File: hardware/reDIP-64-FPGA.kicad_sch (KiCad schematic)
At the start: 22 parts, among them J3 Conn_01x20, J4 Conn_01x20, J5 Conn_01x20, J6 Conn_01x20, J7 Conn_01x20, U16 SN74CBTD16211DGVR, U17 SN74CBTD16211DGVR, U18 SN74CBTD16211DGVR, U19 SN74CBTD16211DGVR, U8 LFE5UM5G-25F-8MG285C

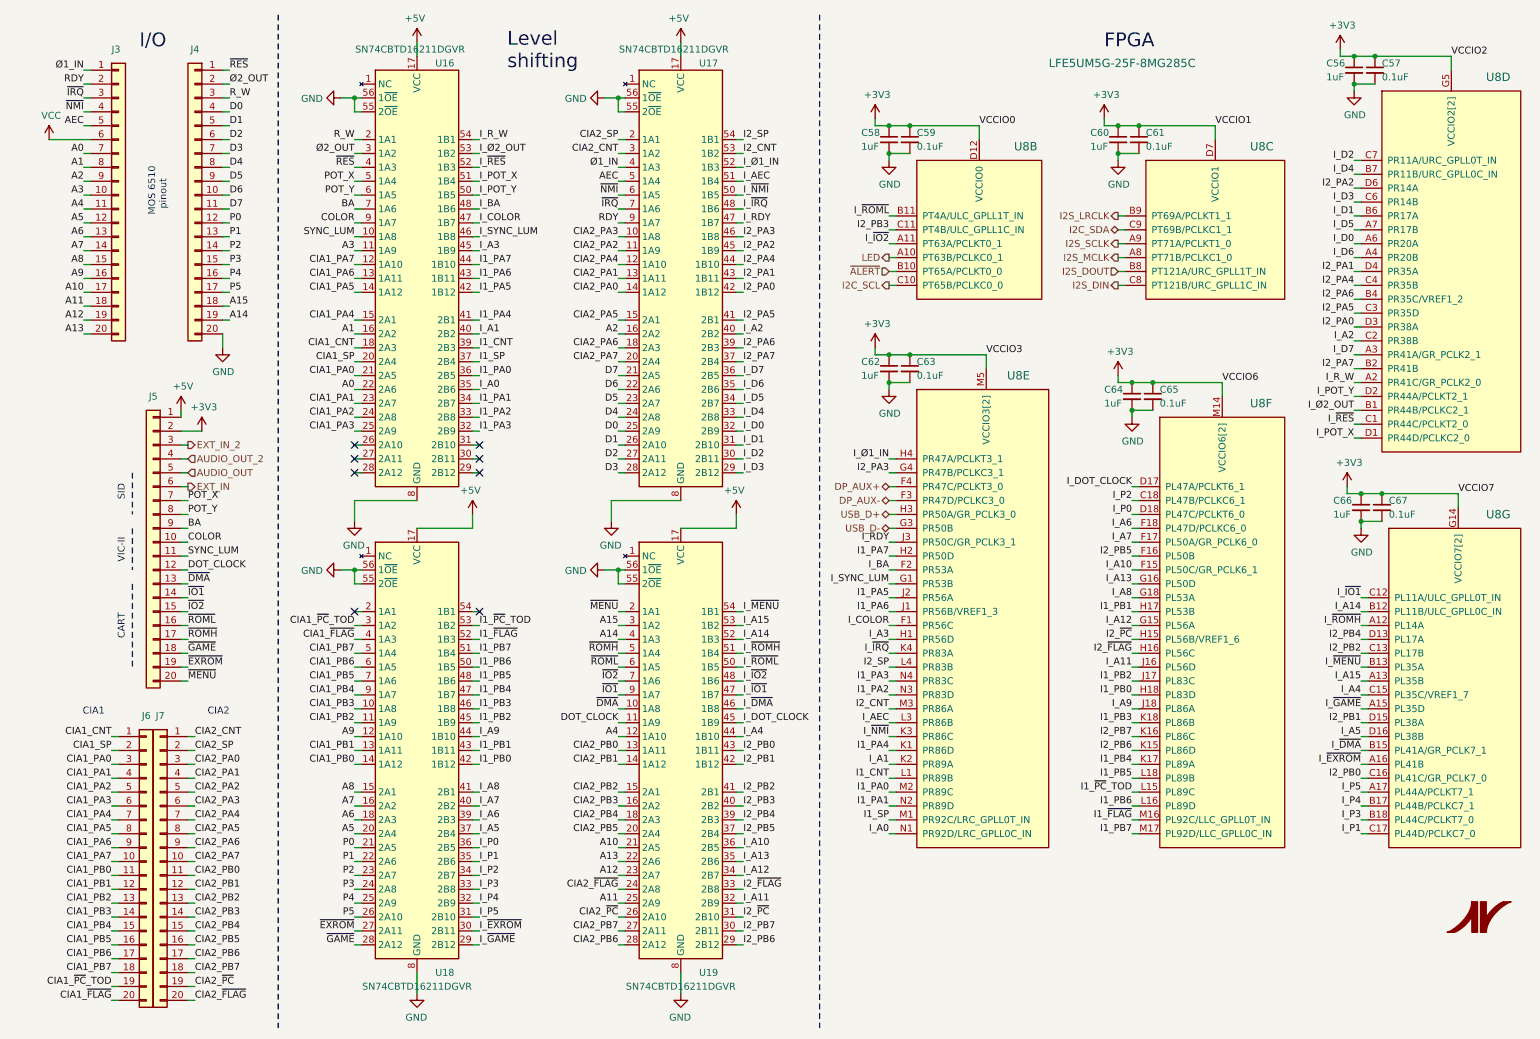
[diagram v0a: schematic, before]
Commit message: Various improvements
* Removed slash from sheet names
* Reannotated schematics
* Example derivation of clocks in schematics
* Identical capacitors for DisplayPort main lanes and AUX
* Replaced switch FSA2259UMX with FSUSB42UMX
* Modified PCB physical stackup to (hopefully) be manufacturable
* Only one microvia size (0.1mm)
* Changed track width for differential pairs
* Routing cleanups and improvements
* Added files for manufacture
* Updated README

Many thanks for advice and help go to @azonenberg, @DX-MON, @gatecat,
@smunaut, and @zyp.
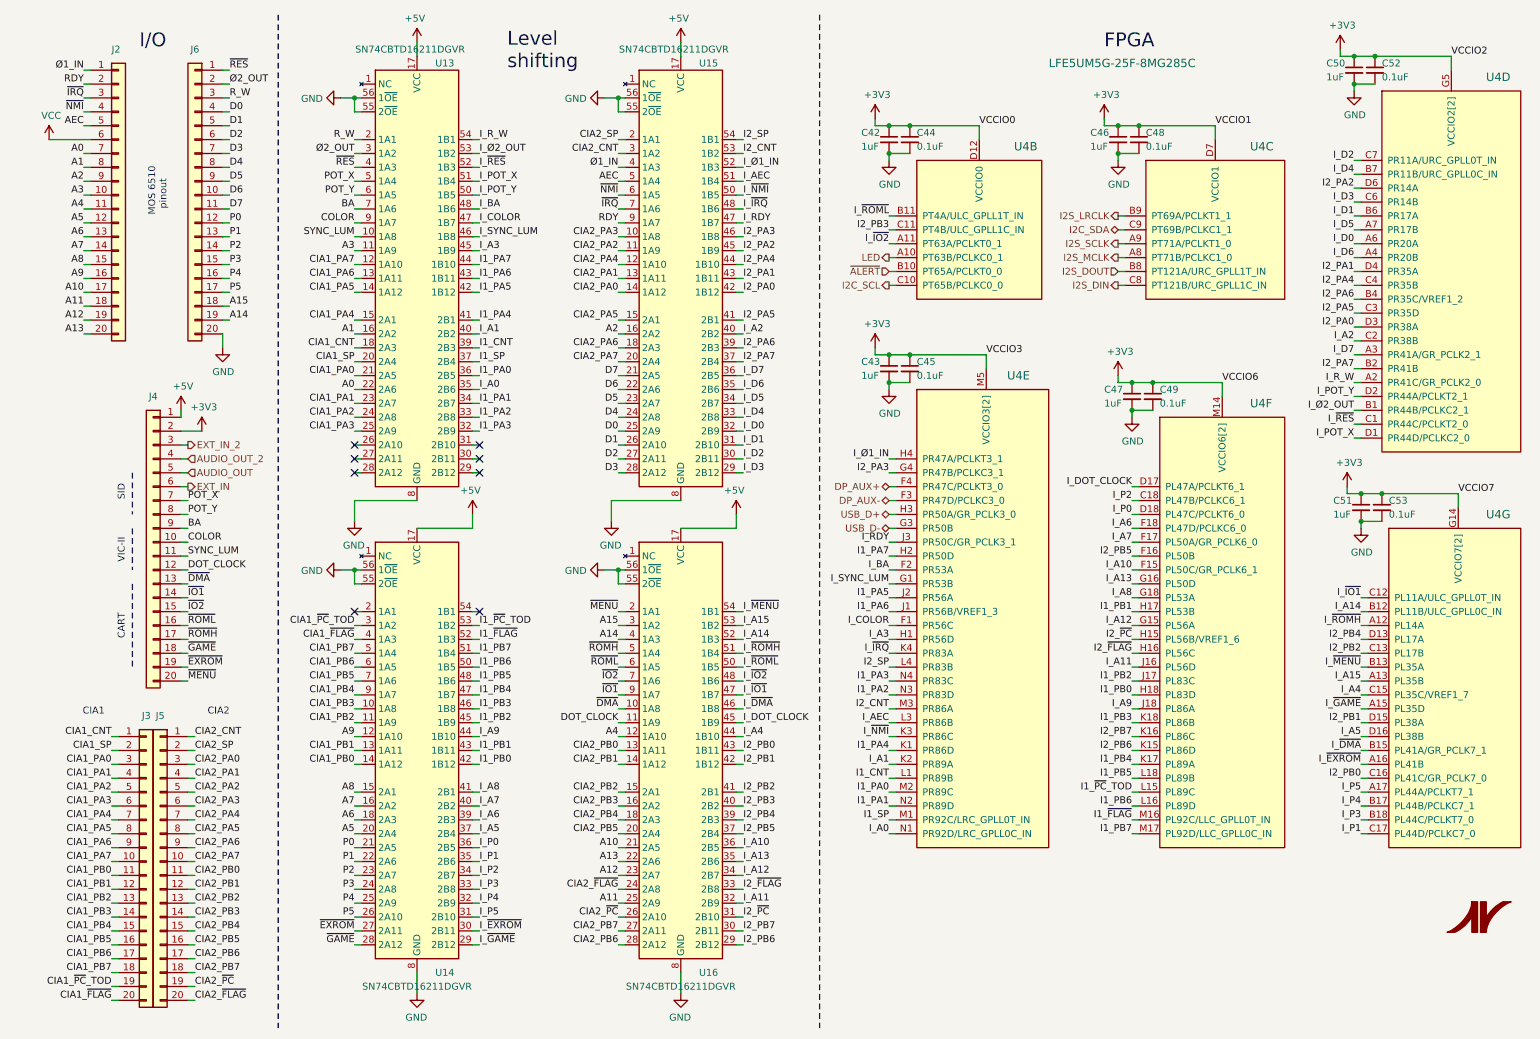
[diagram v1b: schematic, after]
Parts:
- renumbered C58 to C42, C62 to C43, C59 to C44, C63 to C45, C60 to C46, C64 to C47, C61 to C48, C65 to C49, C56 to C50, C66 to C51, C57 to C52, C67 to C53, J3 to J2, J6 to J3, J5 to J4, J7 to J5, J4 to J6, U16 to U13, U18 to U14, U17 to U15, U19 to U16, U8 to U4

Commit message: Updated all KiCad files to current format
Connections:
- net CIA1_~FLAG~ renamed CIA1_~{FLAG}
- net CIA1_~PC~_TOD renamed CIA1_~{PC}_TOD
- net CIA2_~FLAG~ renamed CIA2_~{FLAG}
- net CIA2_~PC~ renamed CIA2_~{PC}
- net I1_~FLAG~ renamed I1_~{FLAG}
- net I1_~PC~_TOD renamed I1_~{PC}_TOD
- net I2_~FLAG~ renamed I2_~{FLAG}
- net I2_~PC~ renamed I2_~{PC}
- net I_~DMA~ renamed I_~{DMA}
- net I_~EXROM~ renamed I_~{EXROM}
- net I_~GAME~ renamed I_~{GAME}
- net I_~IO1~ renamed I_~{IO1}
- net I_~IO2~ renamed I_~{IO2}
- net I_~IRQ~ renamed I_~{IRQ}
- net I_~MENU~ renamed I_~{MENU}
- net I_~NMI~ renamed I_~{NMI}
- net I_~RES~ renamed I_~{RES}
- net I_~ROMH~ renamed I_~{ROMH}
- net I_~ROML~ renamed I_~{ROML}
- net ~ALERT~ renamed ~{ALERT}
- net ~DMA~ renamed ~{DMA}
- net ~EXROM~ renamed ~{EXROM}
- net ~GAME~ renamed ~{GAME}
- net ~IO1~ renamed ~{IO1}
- net ~IO2~ renamed ~{IO2}
- net ~IRQ~ renamed ~{IRQ}
- net ~MENU~ renamed ~{MENU}
- net ~NMI~ renamed ~{NMI}
- net ~RES~ renamed ~{RES}
- net ~ROMH~ renamed ~{ROMH}
- net ~ROML~ renamed ~{ROML}

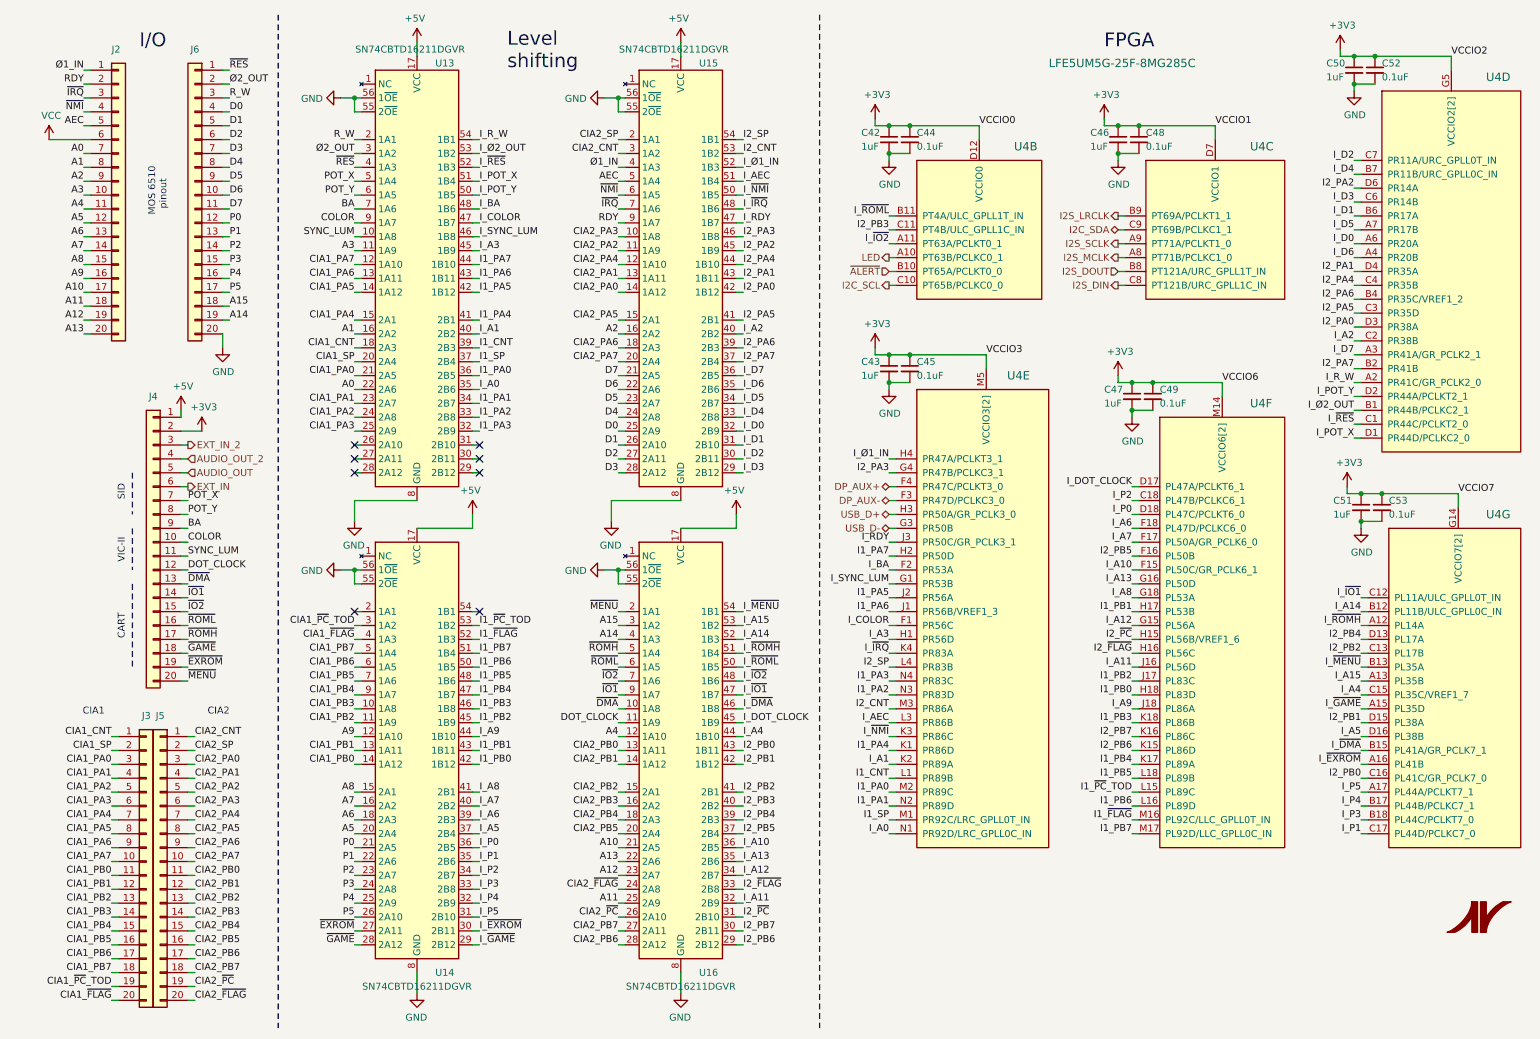
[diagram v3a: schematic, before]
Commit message: Revision 1.0
* USB receptacle replaced with GCT USB4080-03-A / HRO TYPE-C-31-M-05
* USB PD TCPC changed to PTN5110NHQ (FPF2286 has 15ms VBUS debounce time)
* Complete rework of power section
  - Over-voltage protection on VBUS (FPF2286 / FPF2495C)
  - Bidirectional VCC (2 x TPS22916)
  - Replaced EOLed buck converters with FAN53610 / FAN53611
  - Replaced EOLed LDO for ECP5 VCCAUX with NCP115AMX250TCG
  - Replaced LDO for SGTL5000 VDDA with 3.3V version
  - Added separate LDO for SGTL5000 VDDD, avoiding overvoltage on ECP5 VCC
* Bus switch changed to SN74CBT16211A, biased for level shifting
* Registered I/O for FLASH / HyperRAM clock
* Pin header changes:
  - Machined (round) pins for MOS6510 socket
  - Top only headers for additional I/O
  - Reworked pinout for VIC-II and SID
  - Removed 5V output (now available on bidirectional VCC)
  - Added GND for audio / 3.3V
  - Changed JTAG pinout to match Tag-Connect TC-LATTICE / TC-XILINX6
* Removed EXT_IN capacitors
* Button force changed from 240gf to 100gf
* Space for UL and date codes
* Black solder mask
* Silk screen updates
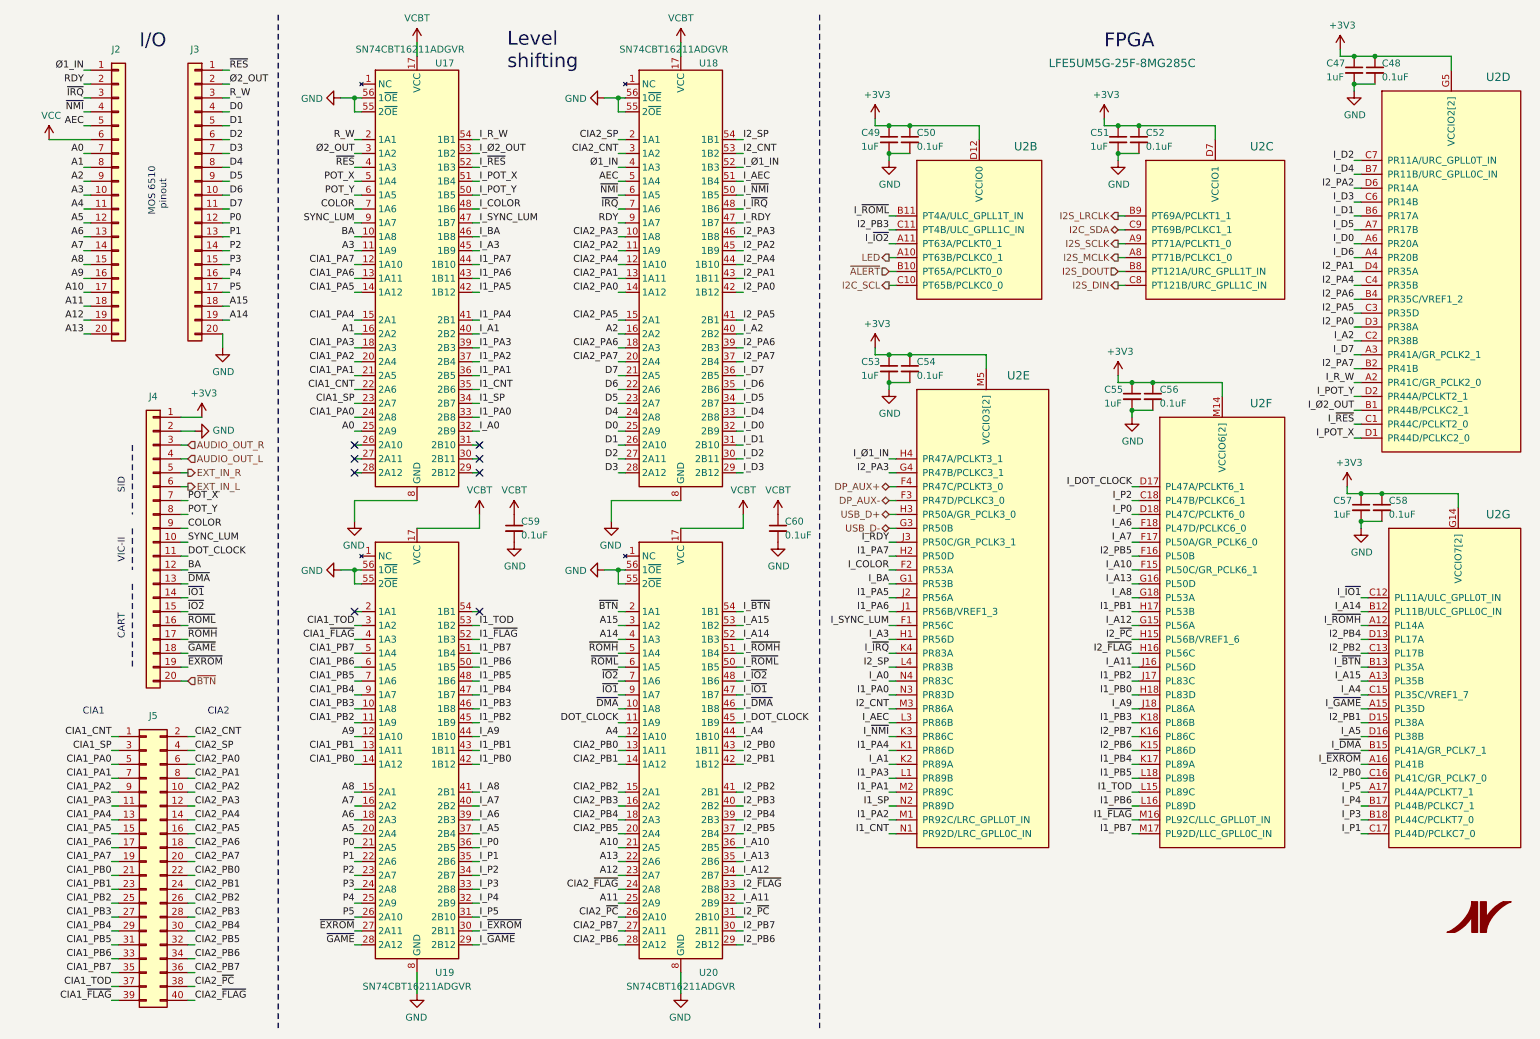
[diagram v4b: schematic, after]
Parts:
- removed J3, J5: Conn_01x20, reDIP:PinHeader_1x20_P2.54mm_Vertical_LongTail, symbol Connector_Generic:Conn_01x20
- added C59, C60: 0.1uF, Capacitor_SMD:C_0201_0603Metric, symbol Device:C_Small
- added J5: Conn_02x20_Odd_Even, reDIP:PinHeader_2x20_P2.54mm_Vertical, symbol Connector_Generic:Conn_02x20_Odd_Even
- J2: footprint reDIP:PinHeader_1x20_P2.54mm_Vertical -> reDIP:PinHeader_1x20_P2.54mm_Vertical_Machined; Mfg Sullins -> (none); PN PRPC020SAAN-RC -> (none)
- J3: renamed from J6; footprint reDIP:PinHeader_1x20_P2.54mm_Vertical -> reDIP:PinHeader_1x20_P2.54mm_Vertical_Machined; Mfg Sullins -> (none); PN PRPC020SAAN-RC -> (none)
- J4: footprint reDIP:PinHeader_1x20_P2.54mm_Vertical_LongTail -> reDIP:PinHeader_1x20_P2.54mm_Vertical; Mfg Sullins -> (none); PN PRPC020SACN-RC -> (none)
- U17: renamed from U13; value SN74CBTD16211DGVR -> SN74CBT16211ADGVR; symbol TI:SN74CBTD16211 -> TI:SN74CBT16211A; Notes (none) -> REPLACEMENT PART: SN74CBT16211CDGVR; PN SN74CBTD16211DGVR -> SN74CBT16211ADGVR
- U18: renamed from U15; value SN74CBTD16211DGVR -> SN74CBT16211ADGVR; symbol TI:SN74CBTD16211 -> TI:SN74CBT16211A; Notes (none) -> REPLACEMENT PART: SN74CBT16211CDGVR; PN SN74CBTD16211DGVR -> SN74CBT16211ADGVR
- U19: renamed from U14; value SN74CBTD16211DGVR -> SN74CBT16211ADGVR; symbol TI:SN74CBTD16211 -> TI:SN74CBT16211A; Notes (none) -> REPLACEMENT PART: SN74CBT16211CDGVR; PN SN74CBTD16211DGVR -> SN74CBT16211ADGVR
- U20: renamed from U16; value SN74CBTD16211DGVR -> SN74CBT16211ADGVR; symbol TI:SN74CBTD16211 -> TI:SN74CBT16211A; Notes (none) -> REPLACEMENT PART: SN74CBT16211CDGVR; PN SN74CBTD16211DGVR -> SN74CBT16211ADGVR
- renumbered C50 to C47, C52 to C48, C42 to C49, C44 to C50, C46 to C51, C48 to C52, C43 to C53, C45 to C54, C47 to C55, C49 to C56, C51 to C57, C53 to C58, U4 to U2
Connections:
- net +3V3: now also J4.1 (Pin_1); no longer J4.2 (Pin_2)
- net A0: now also U17.25 (2A9); no longer U17.22 (2A6)
- net BA: now also J4.12 (Pin_12), U17.10 (1A8); no longer J4.9 (Pin_9), U17.7 (1A6)
- net CIA1_CNT: now also U17.22 (2A6), J5.1 (Pin_1); no longer U17.18 (2A3)
- net CIA1_PA0: now also U17.24 (2A8), J5.5 (Pin_5); no longer U17.21 (2A5)
- net CIA1_PA1: now also U17.21 (2A5), J5.7 (Pin_7); no longer U17.23 (2A7)
- net CIA1_PA2: now also U17.20 (2A4), J5.9 (Pin_9); no longer U17.24 (2A8)
- net CIA1_PA3: now also U17.18 (2A3), J5.11 (Pin_11); no longer U17.25 (2A9)
- net CIA1_PA4: now also J5.13 (Pin_13)
- net CIA1_PA5: now also J5.15 (Pin_15)
- net CIA1_PA6: now also J5.17 (Pin_17)
- net CIA1_PA7: now also J5.19 (Pin_19)
- net CIA1_PB0: now also J5.21 (Pin_21)
- net CIA1_PB1: now also J5.23 (Pin_23)
- net CIA1_PB2: now also J5.25 (Pin_25)
- net CIA1_PB3: now also J5.27 (Pin_27)
- net CIA1_PB4: now also J5.29 (Pin_29)
- net CIA1_PB5: now also J5.31 (Pin_31)
- net CIA1_PB6: now also J5.33 (Pin_33)
- net CIA1_PB7: now also J5.35 (Pin_35)
- net CIA1_SP: now also U17.23 (2A7), J5.3 (Pin_3); no longer U17.20 (2A4)
- net CIA1_~{FLAG}: now also J5.39 (Pin_39)
- net CIA2_CNT: now also J5.2 (Pin_2)
- net CIA2_PA0: now also J5.6 (Pin_6)
- net CIA2_PA1: now also J5.8 (Pin_8)
- net CIA2_PA2: now also J5.10 (Pin_10)
- net CIA2_PA3: now also J5.12 (Pin_12)
- net CIA2_PA4: now also J5.14 (Pin_14)
- net CIA2_PA5: now also J5.16 (Pin_16)
- net CIA2_PA6: now also J5.18 (Pin_18)
- net CIA2_PA7: now also J5.20 (Pin_20)
- net CIA2_PB0: now also J5.22 (Pin_22)
- net CIA2_PB1: now also J5.24 (Pin_24)
- net CIA2_PB2: now also J5.26 (Pin_26)
- net CIA2_PB3: now also J5.28 (Pin_28)
- net CIA2_PB4: now also J5.30 (Pin_30)
- net CIA2_PB5: now also J5.32 (Pin_32)
- net CIA2_PB6: now also J5.34 (Pin_34)
- net CIA2_PB7: now also J5.36 (Pin_36)
- net CIA2_SP: now also J5.4 (Pin_4)
- net CIA2_~{FLAG}: now also J5.40 (Pin_40)
- net CIA2_~{PC}: now also J5.38 (Pin_38)
- net COLOR: now also J4.9 (Pin_9), U17.7 (1A6); no longer J4.10 (Pin_10), U17.9 (1A7)
- net DOT_CLOCK: now also J4.11 (Pin_11); no longer J4.12 (Pin_12)
- net GND: now also J4.2 (Pin_2), C59.2, C60.2
- net I1_CNT: now also U17.35 (2B6), U2.N1 (PR92D/LRC_GPLL0C_IN); no longer U17.39 (2B3), U2.L1 (PR89B)
- net I1_PA0: now also U17.33 (2B8), U2.N3 (PR83D); no longer U17.36 (2B5), U2.M2 (PR89C)
- net I1_PA1: now also U17.36 (2B5), U2.M2 (PR89C); no longer U17.34 (2B7), U2.N2 (PR89D)
- net I1_PA2: now also U17.37 (2B4), U2.M1 (PR92C/LRC_GPLL0T_IN); no longer U17.33 (2B8), U2.N3 (PR83D)
- net I1_PA3: now also U17.39 (2B3), U2.L1 (PR89B); no longer U17.32 (2B9), U2.N4 (PR83C)
- net I1_SP: now also U17.34 (2B7), U2.N2 (PR89D); no longer U17.37 (2B4), U2.M1 (PR92C/LRC_GPLL0T_IN)
- net I_A0: now also U17.32 (2B9), U2.N4 (PR83C); no longer U17.35 (2B6), U2.N1 (PR92D/LRC_GPLL0C_IN)
- net I_BA: now also U17.46 (1B8), U2.G1 (PR53B); no longer U17.48 (1B6), U2.F2 (PR53A)
- net I_COLOR: now also U17.48 (1B6), U2.F2 (PR53A); no longer U17.47 (1B7), U2.F1 (PR56C)
- net I_SYNC_LUM: now also U17.47 (1B7), U2.F1 (PR56C); no longer U17.46 (1B8), U2.G1 (PR53B)
- net SYNC_LUM: now also J4.10 (Pin_10), U17.9 (1A7); no longer J4.11 (Pin_11), U17.10 (1A8)
- net +5V renamed VCBT
- net VCBT: now also C59.1, C60.1; no longer J4.1 (Pin_1)
- net AUDIO_OUT renamed EXT_IN_R
- net AUDIO_OUT_2 renamed AUDIO_OUT_L
- net CIA1_~{PC}_TOD renamed CIA1_TOD
- net CIA1_TOD: now also J5.37 (Pin_37)
- net EXT_IN renamed EXT_IN_L
- net EXT_IN_2 renamed AUDIO_OUT_R
- net I1_~{PC}_TOD renamed I1_TOD
- net I_~{MENU} renamed I_~{BTN}
- net ~{MENU} renamed ~{BTN}
